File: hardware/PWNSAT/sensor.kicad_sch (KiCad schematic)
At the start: 0 parts

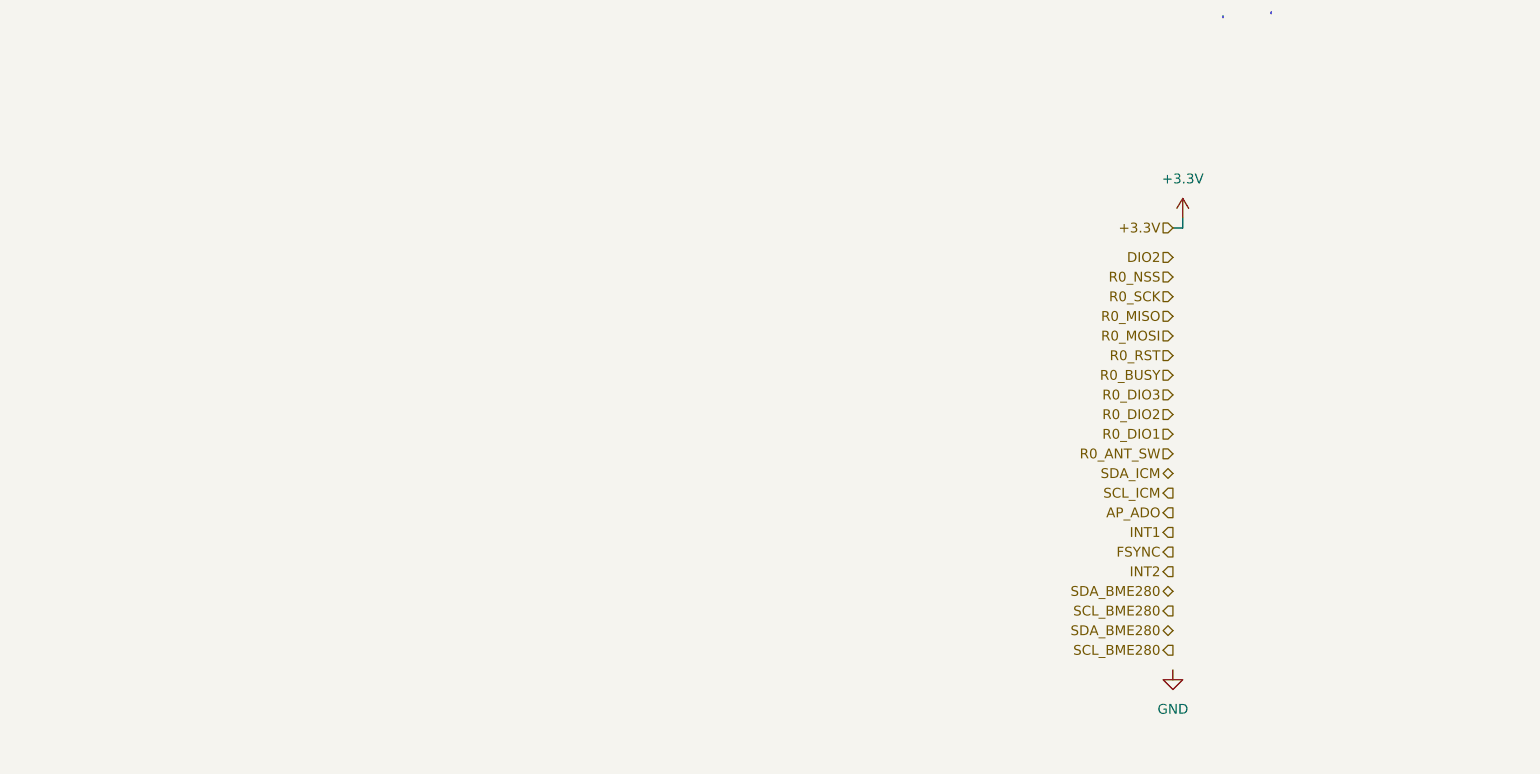
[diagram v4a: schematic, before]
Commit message: feat(Hw):Update_Floorplan_Init_First _route
Pending_Battery_Type
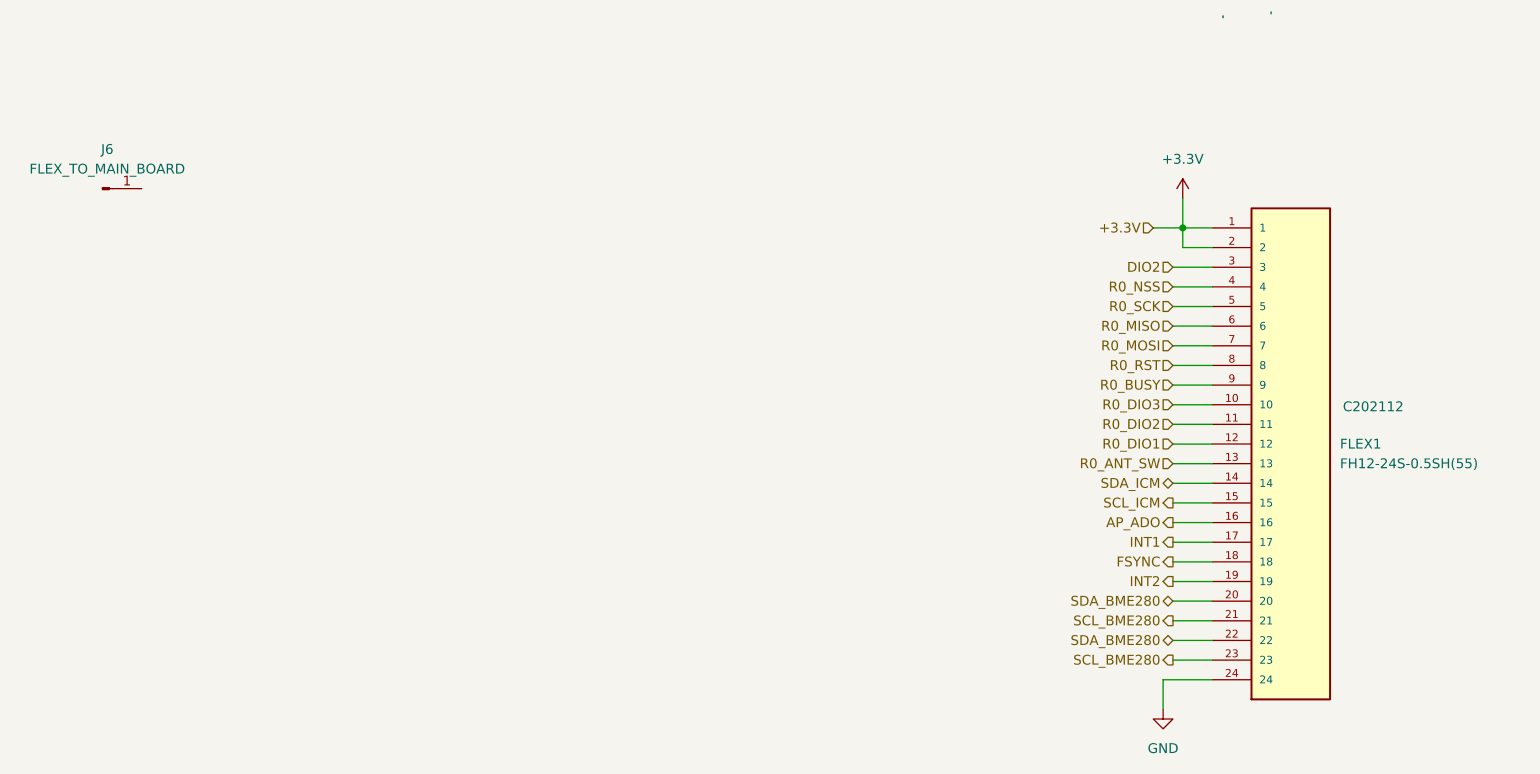
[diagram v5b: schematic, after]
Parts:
- added FLEX1: FH12-24S-0.5SH(55), Connector_FFC-FPC:Hirose_FH12-24S-0.5SH_1x24-1MP_P0.50mm_Horizontal, symbol F31L-1A7H1-11024:F31L-1A7H1-11024
- added J6: FLEX_TO_MAIN_BOARD, symbol Connector:Conn_01x01_Pin
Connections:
- net +3.3V: now also FLEX1.1, FLEX1.2
- net AP_ADO: now also FLEX1.16
- net DIO2: now also FLEX1.3
- net FSYNC: now also FLEX1.18
- net GND: now also FLEX1.24
- net INT1: now also FLEX1.17
- net INT2: now also FLEX1.19
- net R0_ANT_SW: now also FLEX1.13
- net R0_BUSY: now also FLEX1.9
- net R0_DIO1: now also FLEX1.12
- net R0_DIO2: now also FLEX1.11
- net R0_DIO3: now also FLEX1.10
- net R0_MISO: now also FLEX1.6
- net R0_MOSI: now also FLEX1.7
- net R0_NSS: now also FLEX1.4
- net R0_RST: now also FLEX1.8
- net R0_SCK: now also FLEX1.5
- net SCL_BME280: now also FLEX1.21, FLEX1.23
- net SCL_ICM: now also FLEX1.15
- net SDA_BME280: now also FLEX1.20, FLEX1.22
- net SDA_ICM: now also FLEX1.14

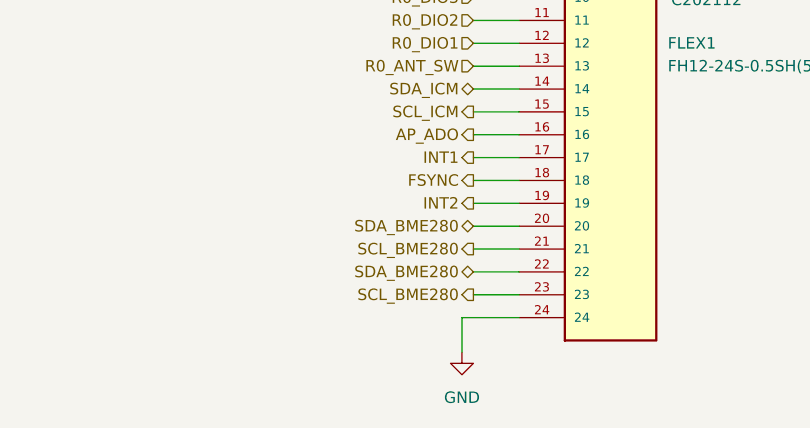
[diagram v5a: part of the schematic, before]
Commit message: feat(Hw):Batt_Board_Pro_Added
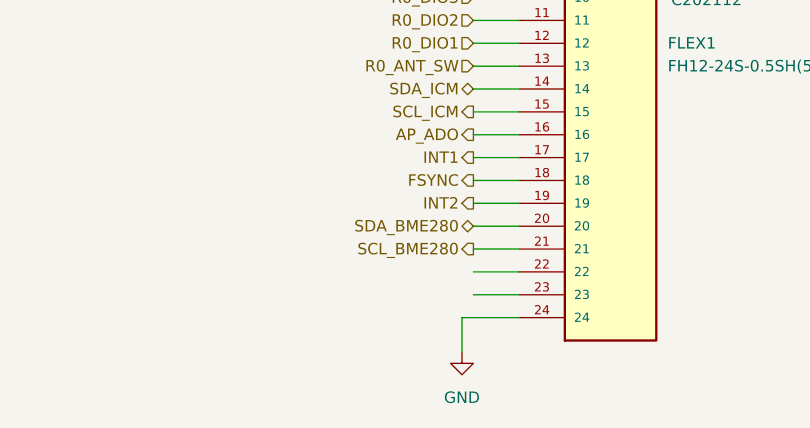
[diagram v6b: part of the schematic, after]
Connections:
- net SCL_BME280: no longer FLEX1.23
- net SDA_BME280: no longer FLEX1.22
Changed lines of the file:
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@@
-		)
-	)
-	(hierarchical_label "SDA_BME280"
-		(shape bidirectional)
-		(at 172.72 99.06 180)
-		(effects
-			(font
-				(size 1.27 1.27)
-			)
-			(justify right)
 		)
 	)
@@
 		(effects
 			(font
-				(size 1.27 1.27)
-			)
-			(justify right)
-		)
-	)
-	(hierarchical_label "SCL_BME280"
-		(shape output)
-		(at 172.72 101.6 180)
-		(effects
-			(font

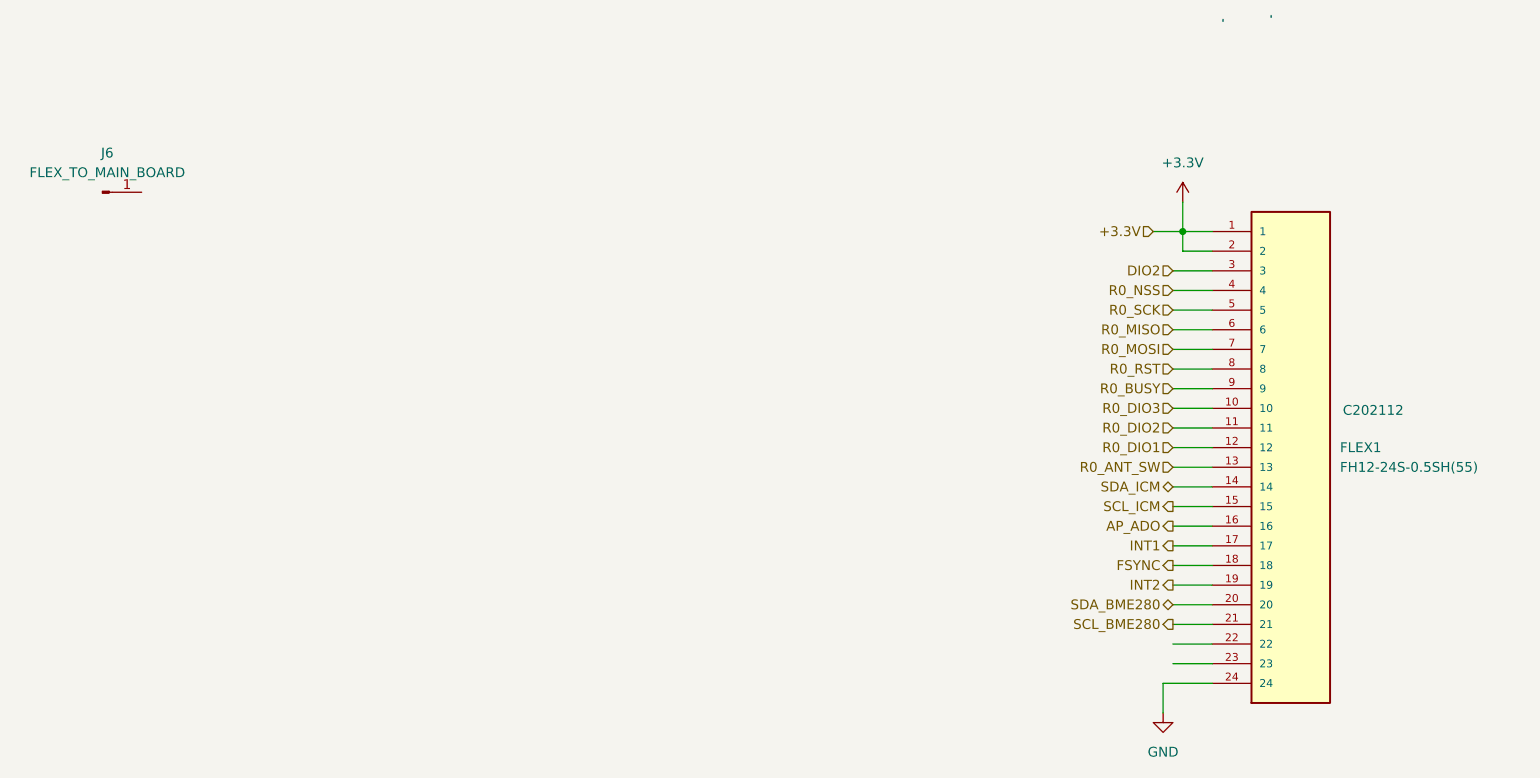
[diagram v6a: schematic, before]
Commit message: feat(Hw):Update_Battery_Sch_And_Sensors_And_PWNCube
pending_Outputs_connectors
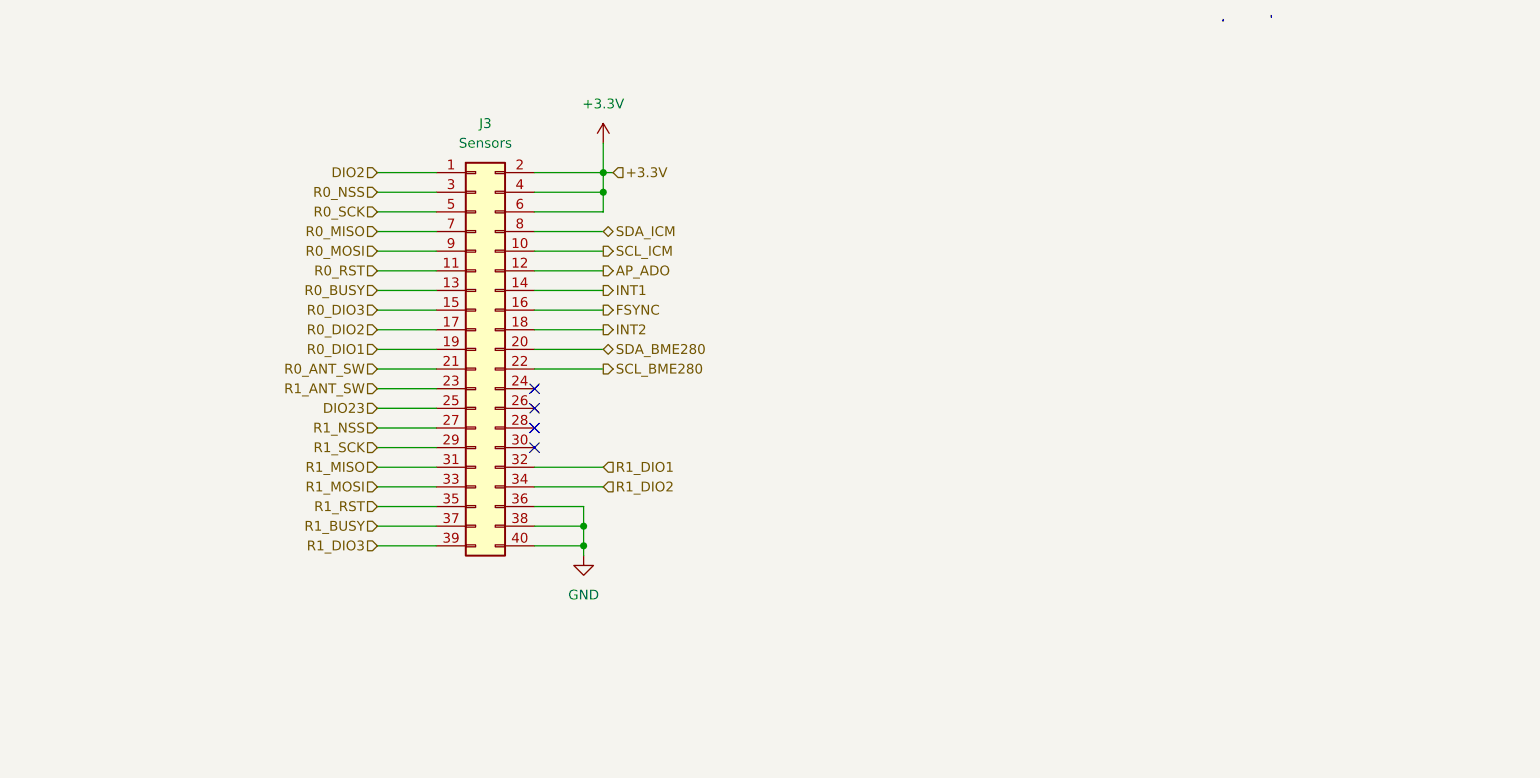
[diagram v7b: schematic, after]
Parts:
- removed FLEX1: FH12-24S-0.5SH(55), Connector_FFC-FPC:Hirose_FH12-24S-0.5SH_1x24-1MP_P0.50mm_Horizontal, symbol F31L-1A7H1-11024:F31L-1A7H1-11024
- removed J6: FLEX_TO_MAIN_BOARD, symbol Connector:Conn_01x01_Pin
- added J3: Sensors, symbol Connector_Generic:Conn_02x20_Odd_Even
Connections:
- net +3.3V: now also J3.2 (Pin_2), J3.4 (Pin_4), J3.6 (Pin_6)
- net AP_ADO: now also J3.12 (Pin_12)
- net DIO2: now also J3.1 (Pin_1)
- net FSYNC: now also J3.16 (Pin_16)
- net GND: now also J3.36 (Pin_36), J3.38 (Pin_38), J3.40 (Pin_40)
- net INT1: now also J3.14 (Pin_14)
- net INT2: now also J3.18 (Pin_18)
- net R0_ANT_SW: now also J3.21 (Pin_21)
- net R0_BUSY: now also J3.13 (Pin_13)
- net R0_DIO1: now also J3.19 (Pin_19)
- net R0_DIO2: now also J3.17 (Pin_17)
- net R0_DIO3: now also J3.15 (Pin_15)
- net R0_MISO: now also J3.7 (Pin_7)
- net R0_MOSI: now also J3.9 (Pin_9)
- net R0_NSS: now also J3.3 (Pin_3)
- net R0_RST: now also J3.11 (Pin_11)
- net R0_SCK: now also J3.5 (Pin_5)
- net SCL_BME280: now also J3.22 (Pin_22)
- net SCL_ICM: now also J3.10 (Pin_10)
- net SDA_BME280: now also J3.20 (Pin_20)
- net SDA_ICM: now also J3.8 (Pin_8)
- new net DIO23: J3.25 (Pin_25)
- new net R1_ANT_SW: J3.23 (Pin_23)
- new net R1_BUSY: J3.37 (Pin_37)
- new net R1_DIO1: J3.32 (Pin_32)
- new net R1_DIO2: J3.34 (Pin_34)
- new net R1_DIO3: J3.39 (Pin_39)
- new net R1_MISO: J3.31 (Pin_31)
- new net R1_MOSI: J3.33 (Pin_33)
- new net R1_NSS: J3.27 (Pin_27)
- new net R1_RST: J3.35 (Pin_35)
- new net R1_SCK: J3.29 (Pin_29)
- no-connect marks 0 -> 4
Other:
- company: (none) -> Electronic Cats
- title: (none) -> PWNCube

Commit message: feat(Hw):floorplans_updated
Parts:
- J3: footprint (none) -> Connector_PinHeader_2.54mm:PinHeader_2x20_P2.54mm_Vertical
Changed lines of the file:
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@@
 			)
 		)
-		(property "Footprint" ""
+		(property "Footprint" "Connector_PinHeader_2.54mm:PinHeader_2x20_P2.54mm_Vertical"
 			(at 82.55 60.96 0)
 			(effects
